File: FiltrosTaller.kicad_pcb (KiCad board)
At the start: 2 copper layers, 21 parts, among them U1 LM741, U2 LM741

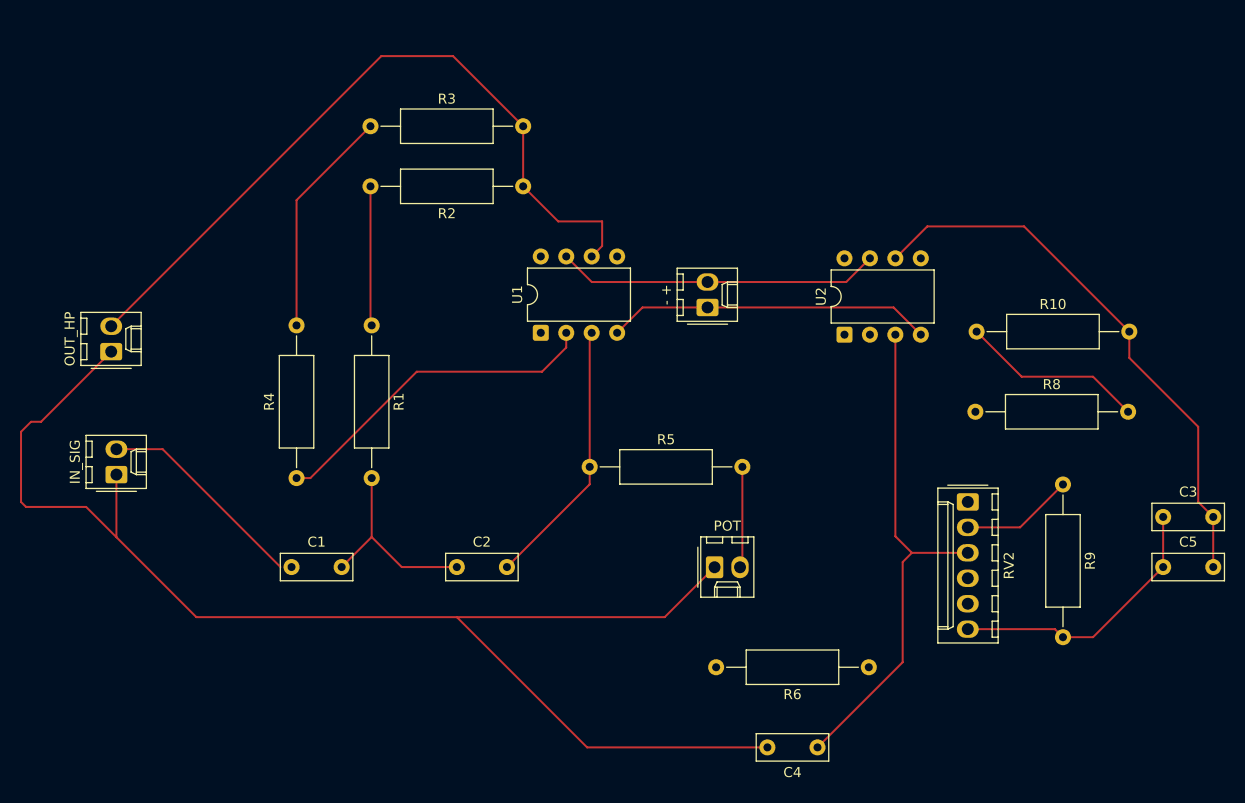
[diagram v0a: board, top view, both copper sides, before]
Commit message: Updated connections
1 layer only
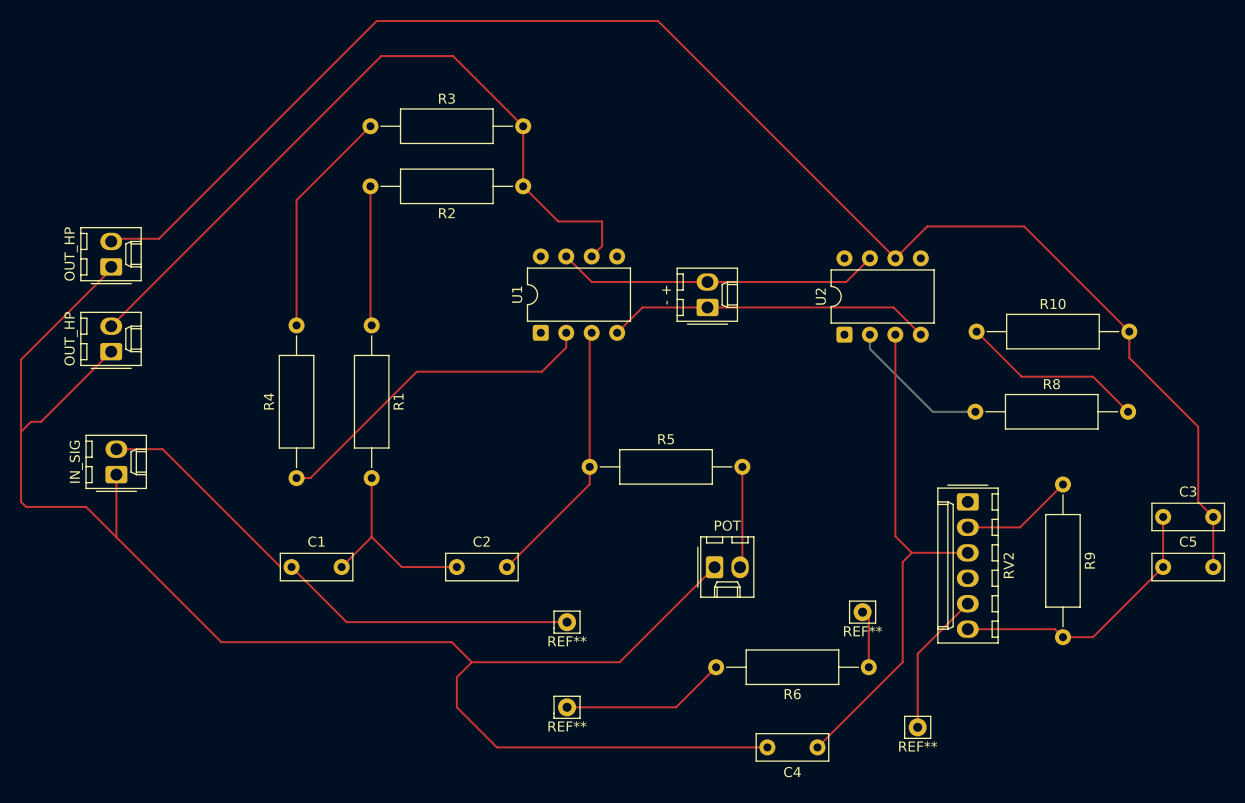
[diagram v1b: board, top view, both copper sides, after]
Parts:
- added OUT_HP: 10k, Connector_Molex:Molex_KK-254_AE-6410-02A_1x02_P2.54mm_Vertical, F.Cu at (106.5, 44.0)
- added REF**: Pin_D0.9mm_L10.0mm_W2.4mm_FlatFork, Connector_Pin:Pin_D0.9mm_L10.0mm_W2.4mm_FlatFork, F.Cu at (187.0, 90.0)
- added REF**: Pin_D0.9mm_L10.0mm_W2.4mm_FlatFork, Connector_Pin:Pin_D0.9mm_L10.0mm_W2.4mm_FlatFork, F.Cu at (152.0, 79.5)
- added REF**: Pin_D0.9mm_L10.0mm_W2.4mm_FlatFork, Connector_Pin:Pin_D0.9mm_L10.0mm_W2.4mm_FlatFork, F.Cu at (152.0, 88.0)
- added REF**: Pin_D0.9mm_L10.0mm_W2.4mm_FlatFork, Connector_Pin:Pin_D0.9mm_L10.0mm_W2.4mm_FlatFork, F.Cu at (181.5, 78.5)
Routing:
- net LP_out: track 56.0 -> 152.6 mm
- net signal: track 0.00 -> 46.3 mm
- net GND: track 138.0 -> 163.8 mm
- net Net-(R6-Pad1): track 0.00 -> 21.0 mm
- net Net-(U2--): track 0.00 -> 14.6 mm
